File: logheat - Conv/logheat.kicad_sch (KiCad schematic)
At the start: 27 parts, among them J1 Conn_01x05_MountingPin, J2 Conn_01x02, J3 Conn_01x04_MountingPin, J4 Conn_01x04_MountingPin, J5 Conn_01x04_MountingPin, J6 Conn_01x02, J7 Conn_01x04_MountingPin, J8 Conn_01x04_MountingPin, J9 Conn_01x04_MountingPin, U1 AD8603AUJZ-R2, U2 MCP3004-I_P, U3 AD8603AUJZ-R2, U4 AD8603AUJZ-R2

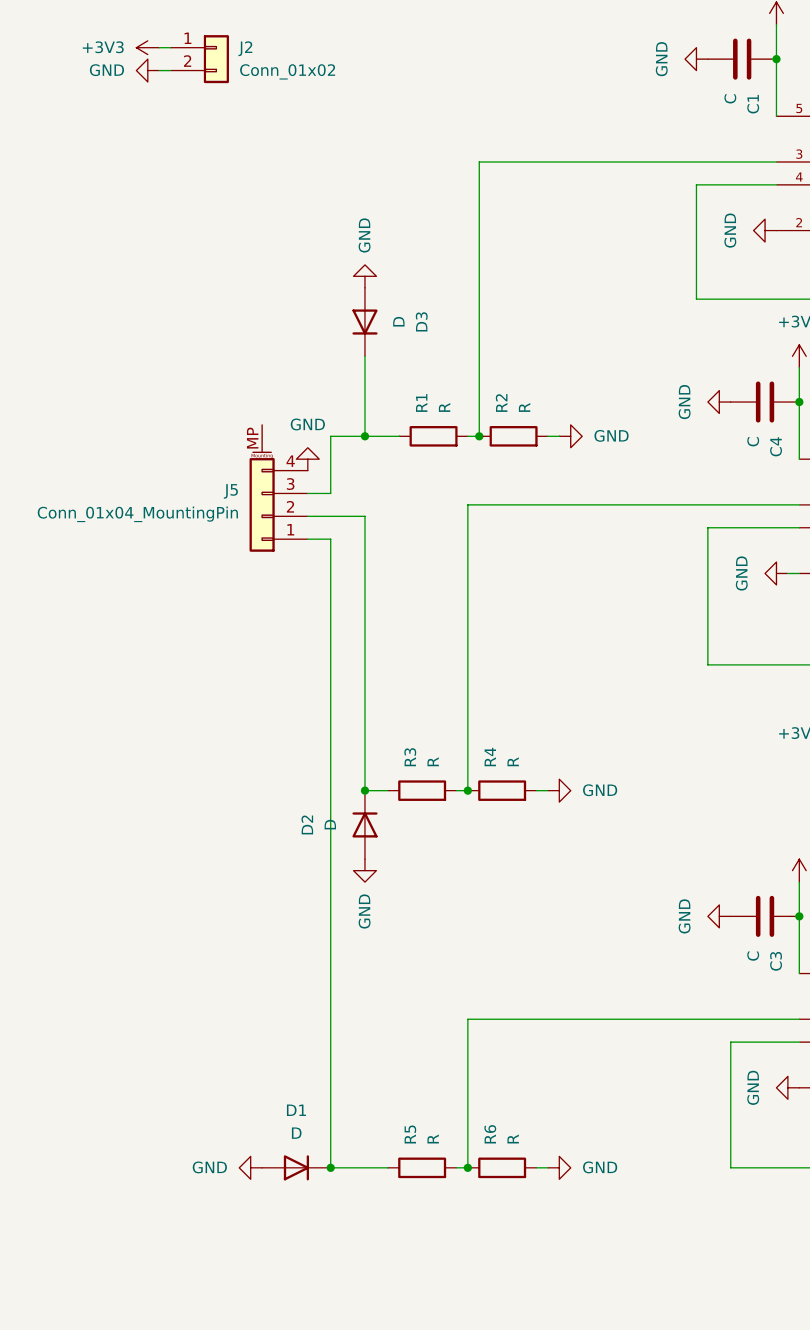
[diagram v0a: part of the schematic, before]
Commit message: Update logheat.kicad_sch
condo pour filtrage des entrées 0-10V
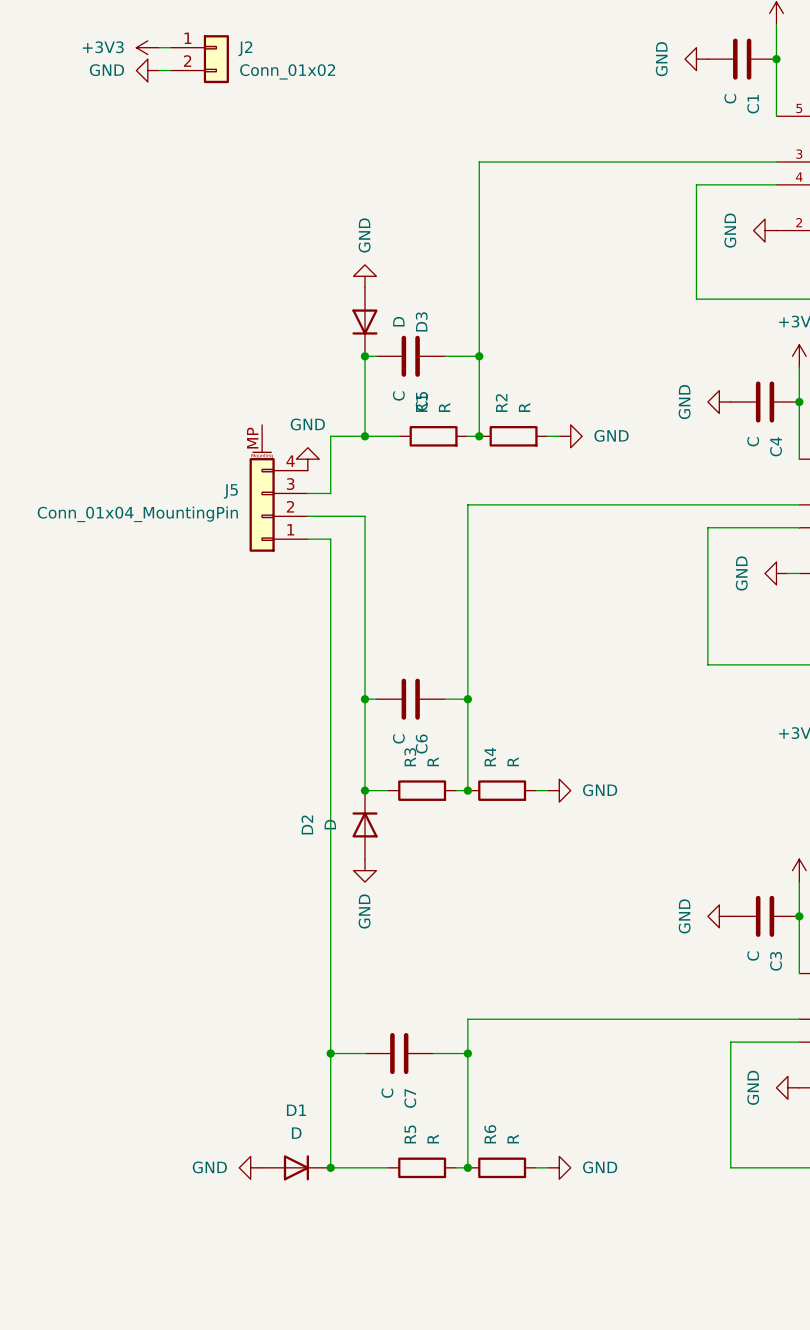
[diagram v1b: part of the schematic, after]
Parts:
- added C5, C6, C7: C, Capacitor_THT:C_Disc_D3.0mm_W1.6mm_P2.50mm, symbol Device:C
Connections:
- net at D1.1 (K), J5.1 (Pin_1), R5.1: now also C7.2
- net at D3.1 (K), J5.3 (Pin_3), R1.1: now also C5.2
- net at R1.2, R2.1, U1.3 (+IN): now also C5.1
- net at D2.1 (K), J5.2 (Pin_2), R3.1: now also C6.2
- net at R3.2, R4.1, U3.3 (+IN): now also C6.1
- net at R5.2, R6.1, U4.3 (+IN): now also C7.1

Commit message: mcp_board
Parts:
- removed J2, J6: Conn_01x02, TerminalBlock:TerminalBlock_MaiXu_MX126-5.0-02P_1x02_P5.00mm, symbol Connector_Generic:Conn_01x02
- removed J7: Conn_01x04_MountingPin, Connector_PinHeader_2.54mm:PinHeader_1x04_P2.54mm_Vertical, symbol Connector_Generic_MountingPin:Conn_01x04_MountingPin
- added J1: Conn_01x06_MountingPin, Connector_PinSocket_2.54mm:PinSocket_1x06_P2.54mm_Vertical, symbol Connector_Generic_MountingPin:Conn_01x06_MountingPin
- added J10: Raspberry_Pi_4, Connector_PinHeader_2.54mm:PinHeader_2x20_P2.54mm_Vertical, symbol Connector:Raspberry_Pi_4
- added J3: Conn_01x02_MountingPin, Connector_PinHeader_2.54mm:PinHeader_1x02_P2.54mm_Vertical, symbol Connector_Generic_MountingPin:Conn_01x02_MountingPin
- J2: renamed from J5; value Conn_01x04_MountingPin -> Analog_inputs
- J4: renamed from J1; value Conn_01x05_MountingPin -> Circuit_conditiono
- J5: renamed from J3; value Conn_01x04_MountingPin -> protec_condit
- J6: renamed from J4; value Conn_01x04_MountingPin -> protec_condit
- J7: renamed from J8; value Conn_01x04_MountingPin -> protec_mcp
- J8: renamed from J9; value Conn_01x04_MountingPin -> protec_mcp
- renumbered C7 to C1, C5 to C2, C6 to C3, C1 to C4, C4 to C5, C3 to C6, C2 to C7, D3 to D2, D2 to D3, R3 to R1, R5 to R2, R1 to R3, R6 to R5, R2 to R6, U3 to U2, U4 to U3, U2 to U4
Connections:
- net +3V3: now also C7.1, R7.2, J10.1 (3V3), J10.17 (3V3), J3.1 (Pin_1); no longer C7.2, R7.1
- net GND: now also C7.2, R7.1, J10.14 (GND), J10.20 (GND), J10.25 (GND), J10.30 (GND), J10.34 (GND), J10.39 (GND), J10.6 (GND), J10.9 (GND), J3.2 (Pin_2); no longer C7.1, R7.2
- net at J6.3 (Pin_3): now also J1.5 (Pin_5), J10.35 (GPIO19/SPI1_MISO/PCM_FS)
- net at J4.4 (Pin_4): now also J1.4 (Pin_4), J10.26 (~{CE1}_SPI0/GPIO07); no longer J5.2 (Pin_2)
- net at J4.5 (Pin_5), U4.11 (CLK): now also J1.1 (Pin_1), J10.23 (SCLK_SPI0/GPIO11)
- net NC: now reaches U4.4 (CH3)
- net at U4.8 (~CS/SHDN): now also J1.3 (Pin_3), J10.24 (~{CE0}_SPI0/GPIO08)
- net at U4.9 (DIN): now also J1.2 (Pin_2), J10.19 (MOSI_SPI0/GPIO10)
- net at J8.3 (Pin_3): now also J1.6 (Pin_6), J10.21 (MISO_SPI0/GPIO09)
- new net: J10.2 (5V), J10.4 (5V)
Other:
- moved on the sheet: C1, C2, C3, C4, C5, C6, C7, D1, D2, D3, J2, J4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
